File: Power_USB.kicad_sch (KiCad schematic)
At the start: 20 parts, among them J1 USB4105-GF-A, U3 AZ1117IH-3.3TRG1, U4 ESD122DMYR

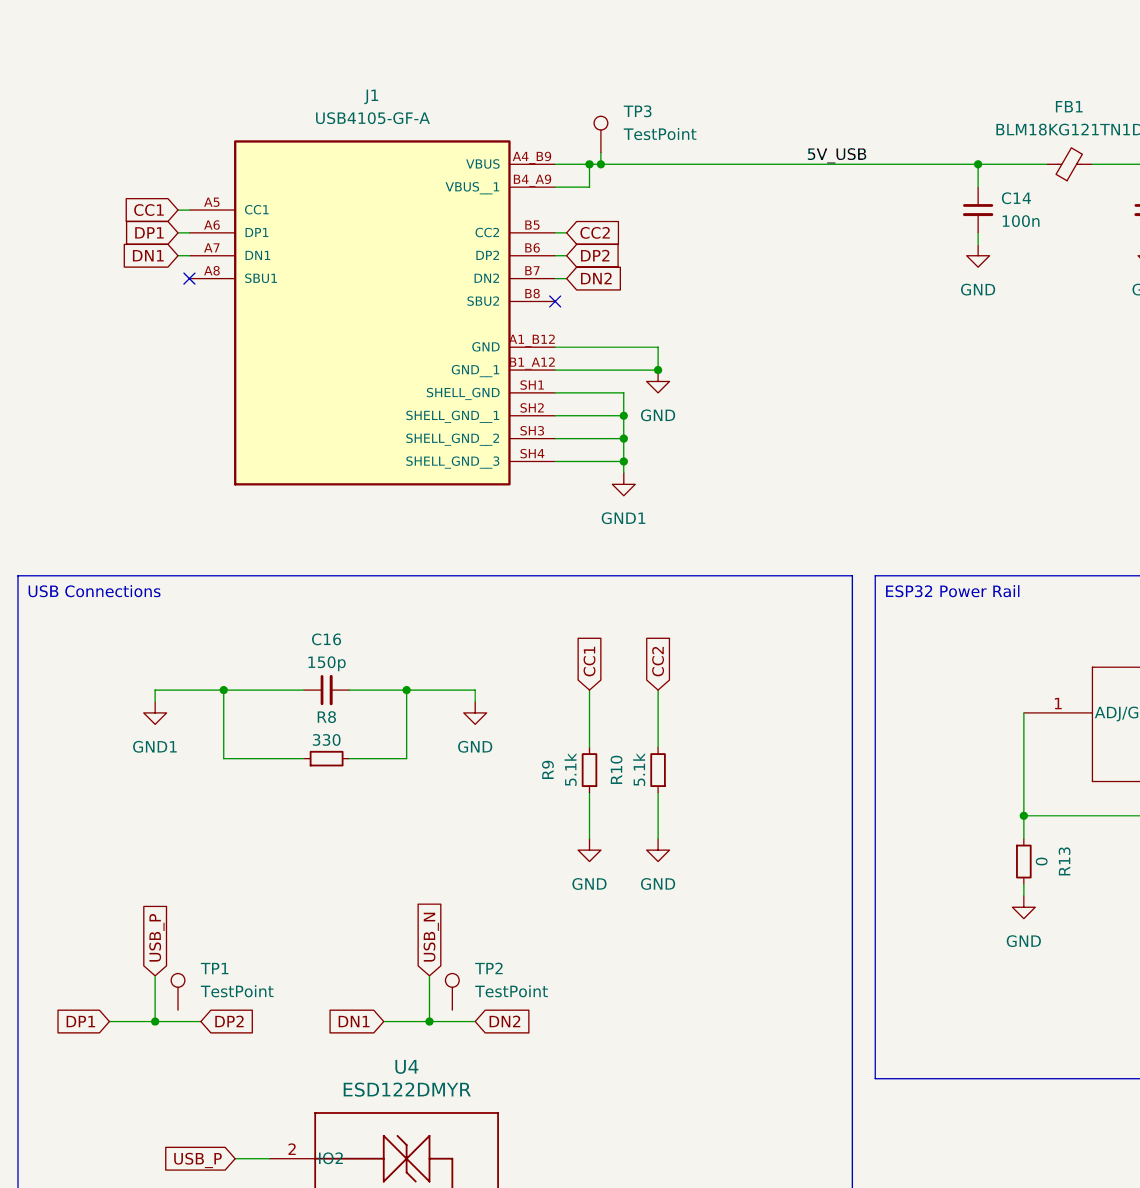
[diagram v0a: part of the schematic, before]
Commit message: -add fuse -change connectors footprint - push button footprint changed
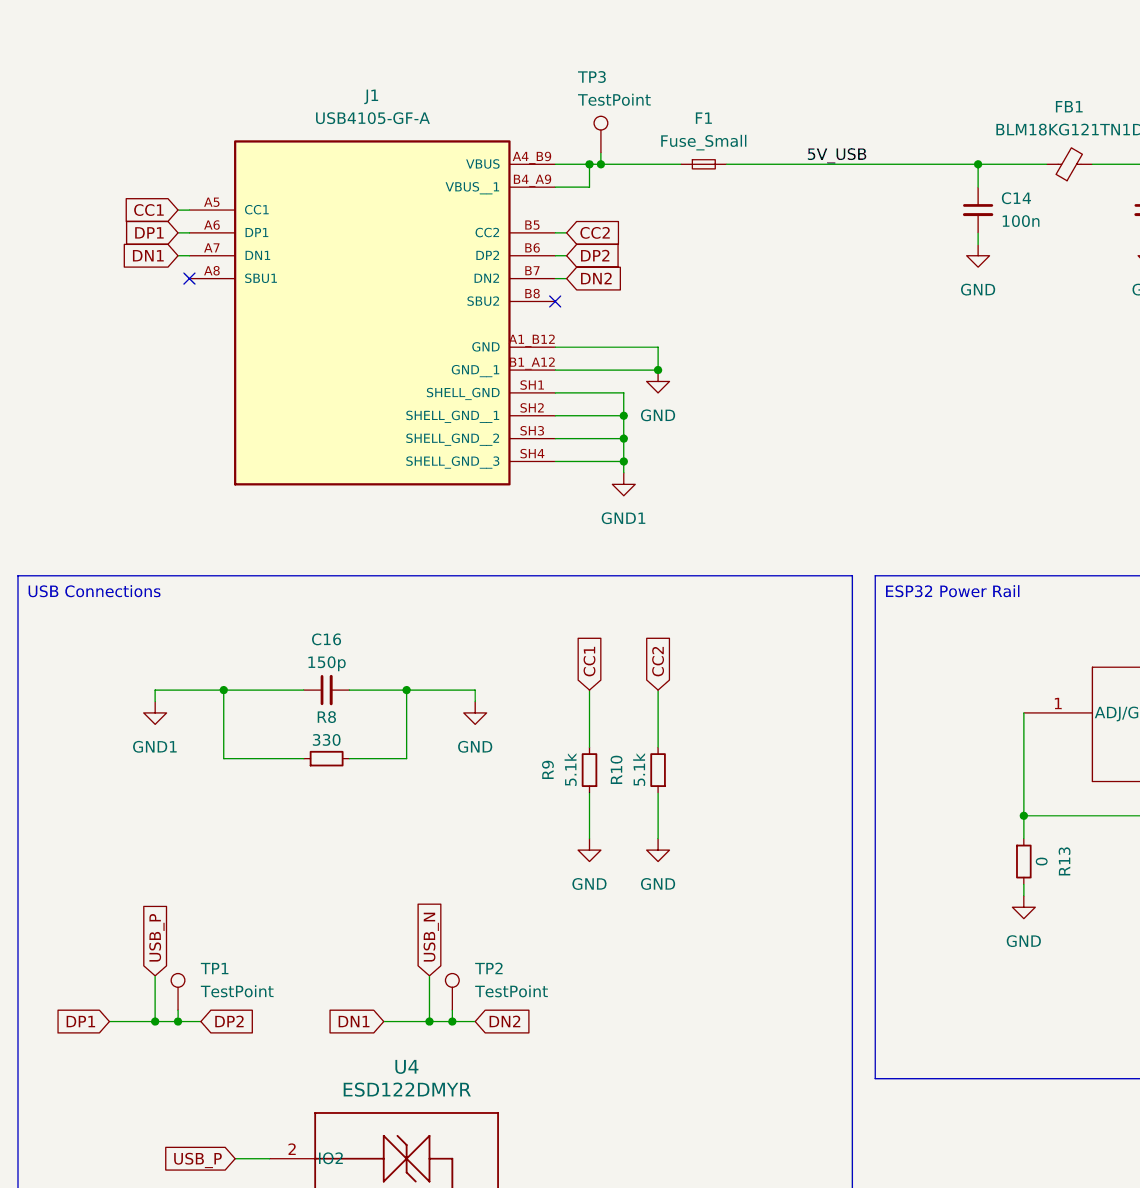
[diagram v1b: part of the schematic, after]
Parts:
- added F1: Fuse_Small, Fuse:Fuse_1206_3216Metric, symbol Device:Fuse_Small
- J1: footprint USB4105-GF-A:GCT_USB4105-GF-A -> 1_ESP32:GCT_USB4105-GF-A
- TP1, TP2, TP3, TP4, TP5: footprint (none) -> TestPoint:TestPoint_Pad_1.5x1.5mm
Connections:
- net 5V_USB: now also F1.2; no longer J1.A4_B9 (VBUS), J1.B4_A9 (VBUS__1), TP3.1
- net DN1: now also TP2.1
- net DP1: now also TP1.1
- new net: F1.1, J1.A4_B9 (VBUS), J1.B4_A9 (VBUS__1), TP3.1
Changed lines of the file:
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@@
 	)
 	(junction
+		(at 36.83 125.73)
+		(diameter 0)
+		(color 0 0 0 0)
+	)
+	(junction
 		(at 34.29 125.73)
 		(diameter 0)
@@
 	)
 	(junction
+		(at 67.31 125.73)
+		(diameter 0)
+		(color 0 0 0 0)
+	)
+	(junction
 		(at 41.91 88.9)
 		(diameter 0)
@@
 	)
 	(junction
-		(at 189.23 93.98)
+		(at 125.73 30.48)
 		(diameter 0)
 		(color 0 0 0 0)
 	)
 	(junction
-		(at 86.36 58.42)
+		(at 83.82 30.48)
 		(diameter 0)
 		(color 0 0 0 0)
 	)
 	(junction
-		(at 64.77 125.73)
+		(at 189.23 93.98)
 		(diameter 0)
 		(color 0 0 0 0)
 	)
 	(junction
-		(at 196.85 100.33)
+		(at 86.36 58.42)
 		(diameter 0)
 		(color 0 0 0 0)
 	)
 	(junction
-		(at 181.61 102.87)
+		(at 64.77 125.73)
 		(diameter 0)
 		(color 0 0 0 0)
 	)
 	(junction
-		(at 86.36 60.96)
+		(at 196.85 100.33)
 		(diameter 0)
 		(color 0 0 0 0)
 	)
 	(junction
-		(at 181.61 93.98)
+		(at 181.61 102.87)
 		(diameter 0)
 		(color 0 0 0 0)
 	)
 	(junction
-		(at 125.73 30.48)
+		(at 86.36 60.96)
 		(diameter 0)
 		(color 0 0 0 0)
 	)
 	(junction
-		(at 83.82 30.48)
+		(at 181.61 93.98)
 		(diameter 0)
 		(color 0 0 0 0)
@@
 	(wire
 		(pts
+			(xy 36.83 125.73) (xy 39.37 125.73)
+		)
+		(stroke
+			(width 0)
+			(type default)
+		)
+	)
+	(wire
+		(pts
 			(xy 83.82 29.21) (xy 83.82 30.48)
 		)
@@
 	(wire
 		(pts
+			(xy 83.82 30.48) (xy 92.71 30.48)
+		)
+		(stroke
+			(width 0)
+			(type default)
+		)
+	)
+	(wire
+		(pts
 			(xy 138.43 30.48) (xy 144.78 30.48)
 		)
@@
 	(wire
 		(pts
-			(xy 34.29 125.73) (xy 39.37 125.73)
+			(xy 34.29 125.73) (xy 36.83 125.73)
 		)
 		(stroke
@@
 	(wire
 		(pts
-			(xy 83.82 30.48) (xy 125.73 30.48)
+			(xy 34.29 88.9) (xy 41.91 88.9)
 		)
 		(stroke
@@
 	(wire
 		(pts
-			(xy 34.29 88.9) (xy 41.91 88.9)
+			(xy 181.61 93.98) (xy 181.61 96.52)
 		)
 		(stroke
@@
 	(wire
 		(pts
-			(xy 181.61 93.98) (xy 181.61 96.52)
+			(xy 36.83 124.46) (xy 36.83 125.73)
 		)
 		(stroke
@@
 	(wire
 		(pts
-			(xy 64.77 125.73) (xy 69.85 125.73)
+			(xy 64.77 125.73) (xy 67.31 125.73)
 		)
 		(stroke
@@
 	(wire
 		(pts
+			(xy 97.79 30.48) (xy 125.73 30.48)
+		)
+		(stroke
+			(width 0)
+			(type default)
+		)
+	)
+	(wire
+		(pts
 			(xy 210.82 99.06) (xy 210.82 97.79)
 		)
@@
 	(wire
 		(pts
+			(xy 67.31 124.46) (xy 67.31 125.73)
+		)
+		(stroke
+			(width 0)
+			(type default)
+		)
+	)
+	(wire
+		(pts
+			(xy 67.31 125.73) (xy 69.85 125.73)
+		)
+		(stroke
+			(width 0)
+			(type default)
+		)
+	)
+	(wire
+		(pts
 			(xy 144.78 30.48) (xy 152.4 30.48)
 		)
@@
 			)
 		)
-		(property "Footprint" "USB4105-GF-A:GCT_USB4105-GF-A"
+		(property "Footprint" "1_ESP32:GCT_USB4105-GF-A"
 			(at 58.42 40.64 0)
 			(effects
@@
 			)
 		)
-		(property "Footprint" ""
+		(property "Footprint" "TestPoint:TestPoint_Pad_1.5x1.5mm"
 			(at 157.48 29.21 0)
 			(effects
@@
 			)
 		)
-		(property "Footprint" ""
+		(property "Footprint" "TestPoint:TestPoint_Pad_1.5x1.5mm"
 			(at 41.91 124.46 0)
 			(effects
@@
 			)
 		)
-		(property "Footprint" ""
+		(property "Footprint" "TestPoint:TestPoint_Pad_1.5x1.5mm"
 			(at 201.93 99.06 0)
 			(effects
@@
 			)
 		)
-		(property "Footprint" ""
+		(property "Footprint" "TestPoint:TestPoint_Pad_1.5x1.5mm"
 			(at 72.39 124.46 0)
 			(effects
@@
 	)
 	(symbol
+		(lib_id "Device:Fuse_Small")
+		(at 95.25 30.48 0)
+		(unit 1)
+		(exclude_from_sim no)
+		(in_bom yes)
+		(on_board yes)
+		(dnp no)
+		(fields_autoplaced yes)
+		(property "Reference" "F1"
+			(at 95.25 25.4 0)
+			(effects
+				(font
+					(size 1.27 1.27)
+				)
+			)
+		)
+		(property "Value" "Fuse_Small"
+			(at 95.25 27.94 0)
+			(effects
+				(font
+					(size 1.27 1.27)
+				)
+			)
+		)
+		(property "Footprint" "Fuse:Fuse_1206_3216Metric"
+			(at 95.25 30.48 0)
+			(effects
+				(font
+					(size 1.27 1.27)
+				)
+				(hide yes)
+			)
+		)
+		(property "Datasheet" "~"
+			(at 95.25 30.48 0)
+			(effects
+				(font
+					(size 1.27 1.27)
+				)
+				(hide yes)
+			)
+		)
+		(property "Description" "Fuse, small symbol"
+			(at 95.25 30.48 0)
+			(effects
+				(font
+					(size 1.27 1.27)
+				)
+				(hide yes)
+			)
+		)
+		(pin "1"
+		)
+		(pin "2"
+		)
+		(instances
+			(project ""
+				(path "/bd736b67-78b5-4b44-8bc5-938ac4442862/eac25d44-a0ca-4267-85ba-7ec959c2971b"
+					(reference "F1")
+					(unit 1)
+				)
+			)
+		)
+	)
+	(symbol
 		(lib_id "power:GND")
 		(at 90.17 105.41 0)
@@
 		(on_board yes)
 		(dnp no)
-		(fields_autoplaced yes)
 		(property "Reference" "TP3"
-			(at 86.36 24.6379 0)
+			(at 81.28 20.828 0)
 			(effects
 				(font
@@
 		)
 		(property "Value" "TestPoint"
-			(at 86.36 27.1779 0)
+			(at 81.28 23.368 0)
 			(effects
 				(font
@@
 			)
 		)
-		(property "Footprint" ""
+		(property "Footprint" "TestPoint:TestPoint_Pad_1.5x1.5mm"
 			(at 88.9 29.21 0)
 			(effects
